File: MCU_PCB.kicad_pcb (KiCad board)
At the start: 2 copper layers, 70 x 70 mm, 51 parts, among them J1 BackBone, J2 D1, J3 D2, J4 Micro_SD_Card, J5 CAM_0, J6 CAM_1, J7 47080-4005, U1 STM32G071GBU, U2 MCP795W22-I/ST, U3 74HCT4051BQ-Q100,1, U4 74HCT4051BQ-Q100,1, U5 ADT7310, U6 LIS2MDLTR, U7 LSM6DSRX, Y1 TG-3541CE

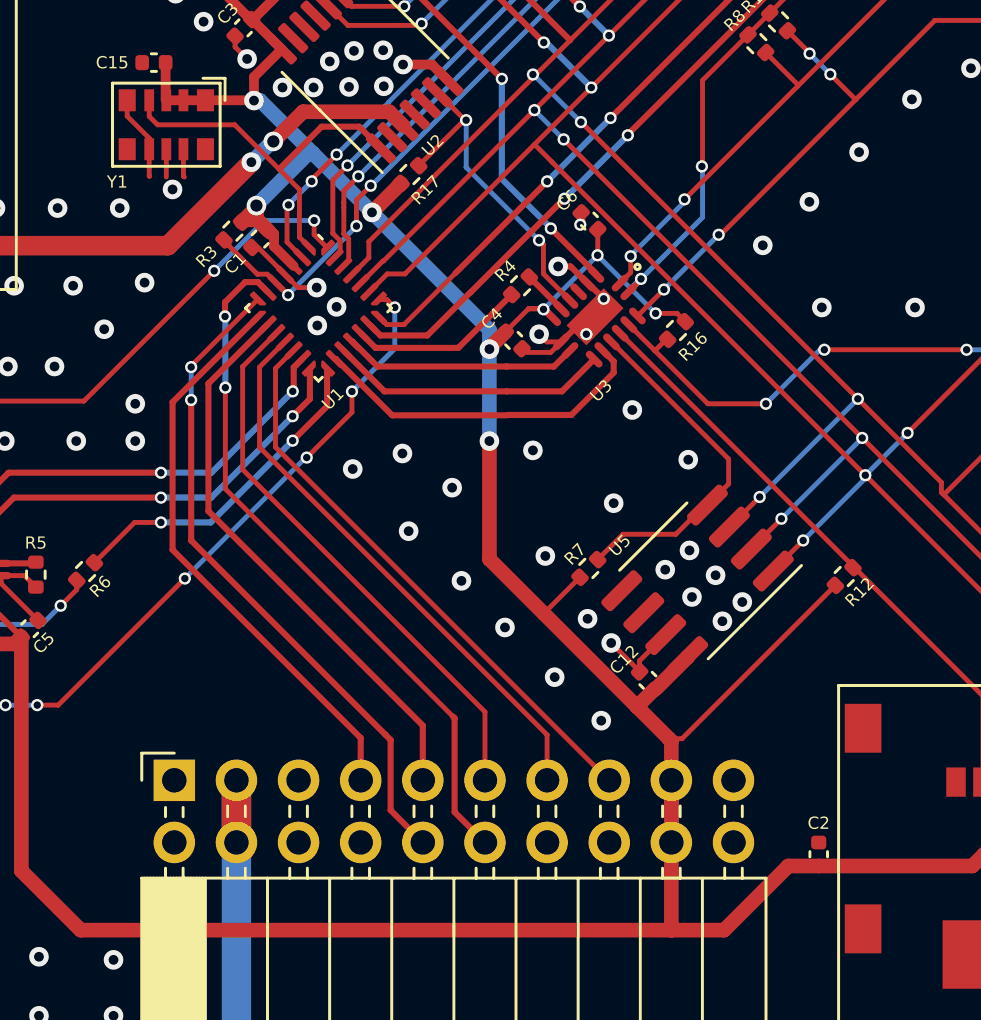
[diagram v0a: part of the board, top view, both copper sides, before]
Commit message: Changed DE-MUX and logic behind it.
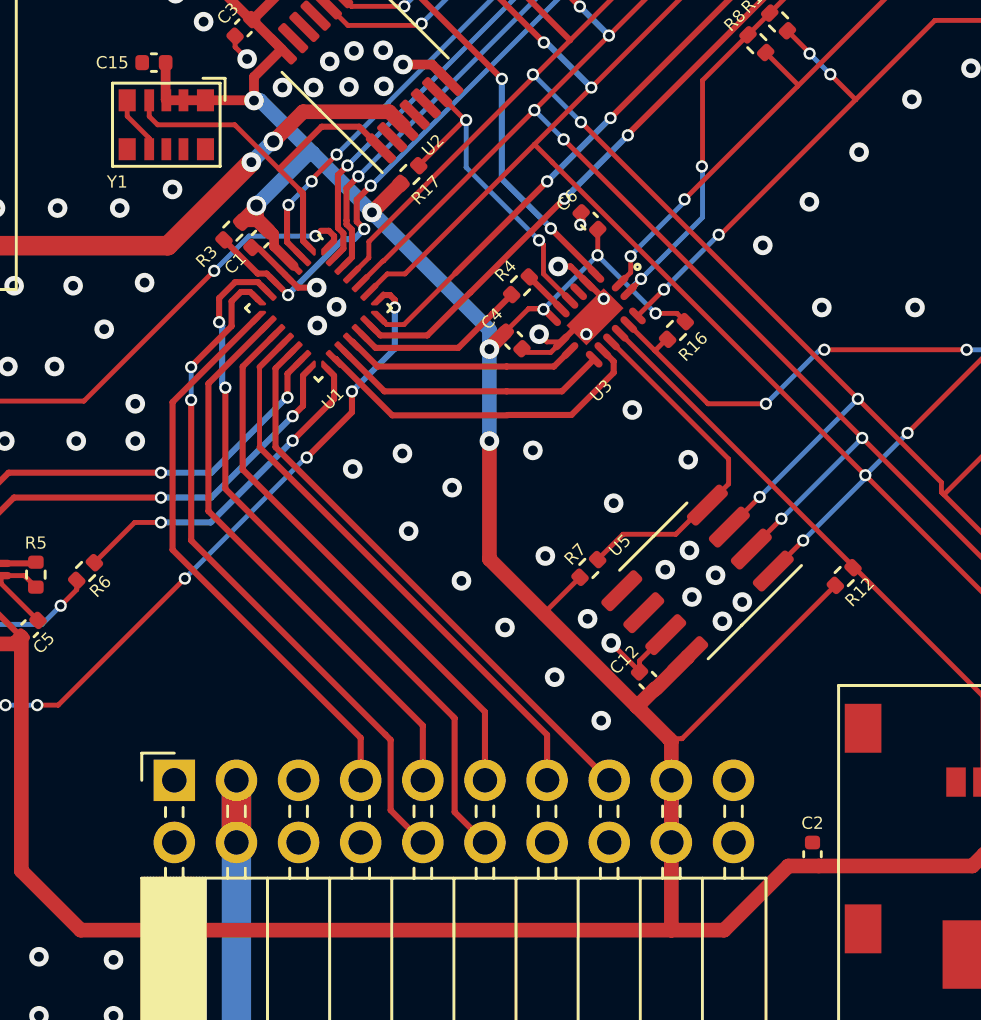
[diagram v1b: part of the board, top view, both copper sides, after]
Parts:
- moved C2 0.25 mm to (142.2, 123.7)
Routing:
- net GND: track 50.3 -> 46.9 mm
- net /IO/COM_RX: track 27.5 -> 28.4 mm
- net /IO/~{RST}: track 36.8 -> 37.5 mm

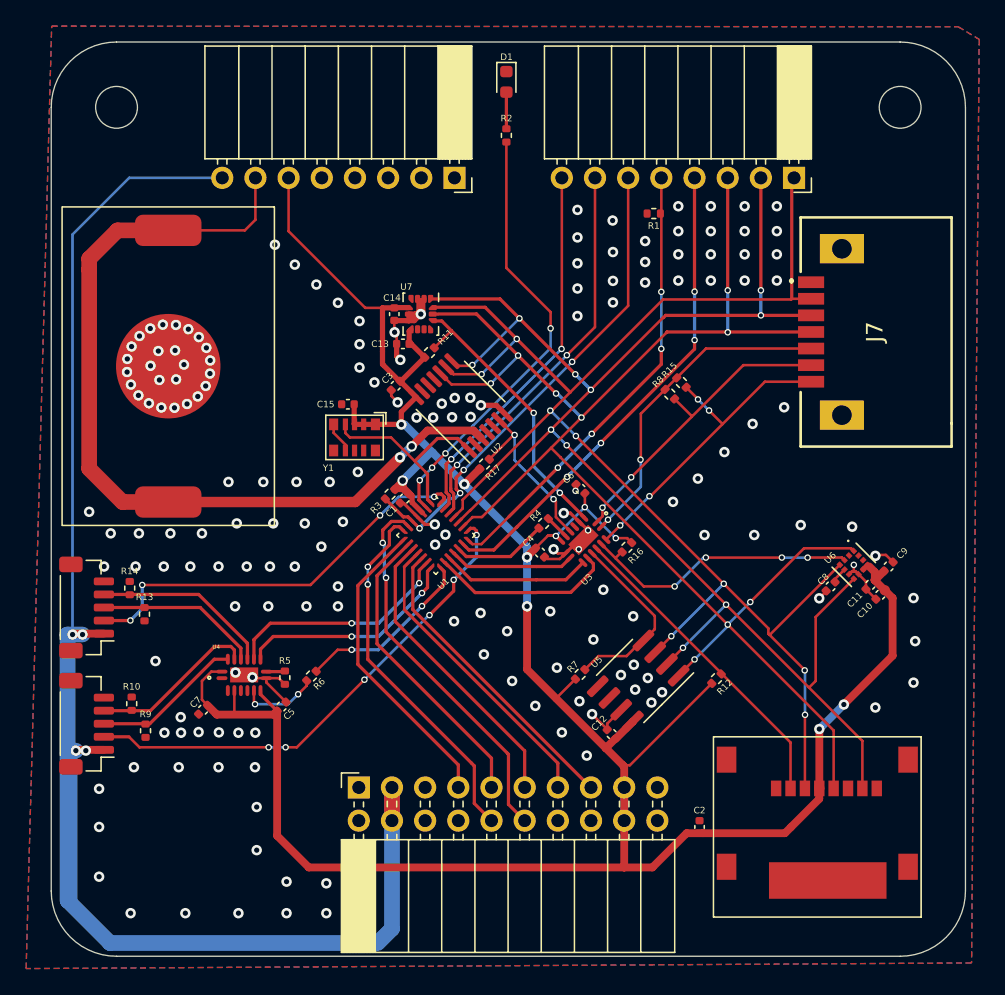
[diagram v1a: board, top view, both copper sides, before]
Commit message: 0.3v KiCad
Needs improvements:
-Visual
-Better grounding
-Component placement
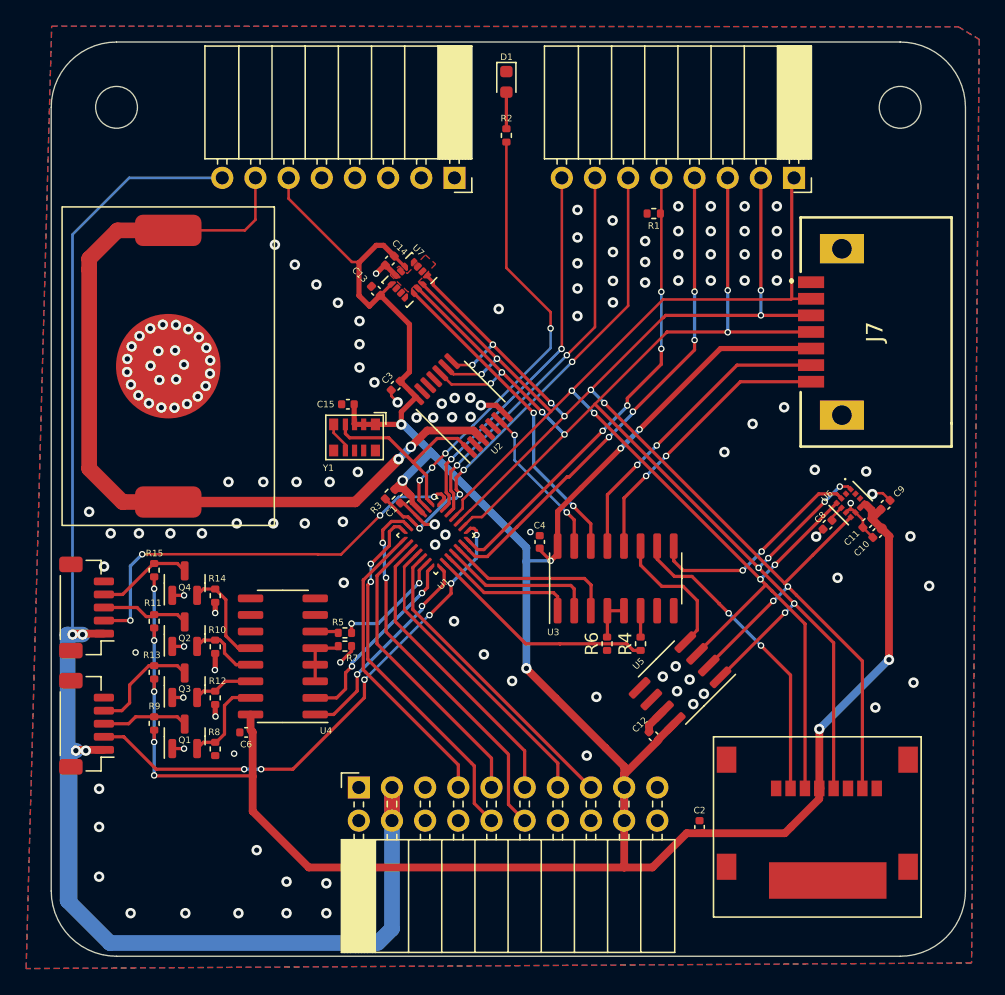
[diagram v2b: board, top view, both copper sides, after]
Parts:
- removed C5, C7: 100nF, Capacitor_SMD:C_0402_1005Metric
- removed R16, R17: 12k, Resistor_SMD:R_0402_1005Metric
- added Q1: RK7002T116, Package_TO_SOT_SMD:SOT-23, F.Cu at (102.8, 116.8)
- added Q2: RK7002T116, Package_TO_SOT_SMD:SOT-23, F.Cu at (102.8, 108.9)
- added Q3: RK7002T116, Package_TO_SOT_SMD:SOT-23, F.Cu at (102.8, 112.8)
- added Q4: RK7002T116, Package_TO_SOT_SMD:SOT-23, F.Cu at (102.8, 105.0)
- U3, U4: value 74HCT4051BQ-Q100,1 -> MC74AC138DR2G; footprint footprints:QFN50P250X350X100-17N -> Package_SO:SOIC-16_3.9x9.9mm_P1.27mm
- moved R8 44.2 mm to (105.2, 117.7), turned to 90 degrees
- moved R15 42.9 mm to (100.5, 104.0), turned to 90 degrees
- moved R12 38.4 mm to (105.2, 113.8), turned to 90 degrees
- moved C6 31.7 mm to (107.5, 116.5), turned to 0 degrees
- moved R11 29.5 mm to (100.5, 108.0), turned to 90 degrees
- moved R6 22.8 mm to (135.2, 109.7), turned to 90 degrees
- moved R7 18.1 mm to (115.1, 109.9), turned to 180 degrees
- moved R4 11.8 mm to (137.7, 109.7), turned to 90 degrees
- moved R10 7.74 mm to (105.2, 109.9), turned to 90 degrees
- moved R14 6.57 mm to (105.2, 106.0), turned to 90 degrees
- moved R5 5.74 mm to (115.1, 108.8), turned to 180 degrees
- moved C10 4.73 mm to (155.8, 101.2)
- moved C11 4.73 mm to (155.1, 100.4)
- moved U6 4.73 mm to (153.8, 98.9)
- moved C8 4.73 mm to (152.0, 100.6)
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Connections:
- C6 pad 1: +3V3 -> GND
- C6 pad 2: GND -> +3V3
- J5 pad 3: /MUX/CAM_ON_0 -> /CAM_SENS/ON/OFF_0
- J5 pad 4: /MUX/CAM_REC_0 -> /CAM_SENS/REC_0
- J6 pad 3: /MUX/CAM_ON_1 -> /CAM_SENS/ON/OFF_1
- J6 pad 4: /MUX/CAM_REC_1 -> /CAM_SENS/REC_1
- J7 pad 6: /MUX/~{BME680_SS} -> /CAM_SENS/~{BME680_SS}
- J7 pad 7: /MUX/~{TEMP_OUT_SS} -> /CAM_SENS/~{TEMP_OUT_SS}
- R10 pad 2: /MUX/CAM_REC_0 -> /MUX/CAM_ON_1_0
- R11 pad 1: /MUX/~{IMU_SS} -> +3V3
- R11 pad 2: +3V3 -> /CAM_SENS/ON/OFF_1
- R12 pad 1: /MUX/~{SD_CARD_SS} -> GND
- R12 pad 2: +3V3 -> /MUX/CAM_REC_0_0
- R13 pad 1: GND -> +3V3
- R13 pad 2: /MUX/CAM_ON_1 -> /CAM_SENS/REC_0
- R14 pad 2: /MUX/CAM_REC_1 -> /MUX/CAM_REC_1_0
- R15 pad 1: /MUX/~{TEMP_OUT_SS} -> +3V3
- R15 pad 2: +3V3 -> /CAM_SENS/REC_1
- R5 pad 1: GND -> /MCU/MUX_EN_1
- R6 pad 1: /MCU/MUX_EN_1 -> GND
- R7 pad 1: /MUX/~{TEMP_IN_SS} -> GND
- R7 pad 2: +3V3 -> Net-(R7-Pad2)
- R8 pad 1: /MUX/~{BME680_SS} -> GND
- R8 pad 2: +3V3 -> /MUX/CAM_ON_0_0
- R9 pad 1: GND -> +3V3
- R9 pad 2: /MUX/CAM_ON_0 -> /CAM_SENS/ON/OFF_0
- U1 pad 13: /MCU/S0_CAM -> /MCU/MUX_EN_1
- U1 pad 15: /MCU/MUX_EN_1 -> /MCU/S0_CAM
- U1 pad 16: /MCU/S0_SENS -> /MCU/MUX_EN_0
- U1 pad 17: /MCU/S1_SENS -> /MCU/S0_SENS
- U1 pad 18: /MCU/S2_SENS -> /MCU/S1_SENS
- U1 pad 19: /MCU/MUX_EN_0 -> /MCU/S2_SENS
- U3 pad 1: /MUX/~{BME680_SS} -> /MCU/S0_SENS
- U3 pad 10: /MCU/S1_SENS -> /MUX/~{SD_CARD_SS}
- U3 pad 11: /MCU/S0_SENS -> /MUX/~{TEMP_IN_SS}
- U3 pad 12: /MUX/~{TEMP_IN_SS} -> /CAM_SENS/~{TEMP_OUT_SS}
- U3 pad 13: /MUX/~{SD_CARD_SS} -> /CAM_SENS/~{BME680_SS}
- U3 pad 14: /MUX/~{MAG_SS} -> /MUX/~{IMU_SS}
- U3 pad 15: /MUX/~{TEMP_OUT_SS} -> /MUX/~{RTC_OUT}
- U3 pad 2: /MUX/~{IMU_SS} -> /MCU/S1_SENS
- U3 pad 3: GND -> /MCU/S2_SENS
- U3 pad 4: unconnected-(U3-Pad4) -> Net-(R6-Pad2)
- U3 pad 5: /MUX/~{RTC_OUT} -> Net-(R6-Pad2)
- U3 pad 7: +3V3 -> unconnected-(U3-Pad7)
- U3 pad 9: /MCU/S2_SENS -> /MUX/~{MAG_SS}
- U4 pad 1: unconnected-(U4-Pad1) -> /MCU/S0_CAM
- U4 pad 10: /MCU/S1_CAM -> unconnected-(U4-Pad10)
- U4 pad 11: /MCU/S0_CAM -> unconnected-(U4-Pad11)
- U4 pad 12: /MUX/CAM_REC_1 -> /MUX/CAM_REC_1_0
- U4 pad 13: /MUX/CAM_ON_1 -> /MUX/CAM_ON_1_0
- U4 pad 14: /MUX/CAM_REC_0 -> /MUX/CAM_REC_0_0
- U4 pad 15: /MUX/CAM_ON_0 -> /MUX/CAM_ON_0_0
- U4 pad 2: unconnected-(U4-Pad2) -> /MCU/S1_CAM
- U4 pad 3: +3V3 -> Net-(R7-Pad2)
- U4 pad 4: unconnected-(U4-Pad4) -> Net-(R7-Pad2)
- U4 pad 5: unconnected-(U4-Pad5) -> Net-(R7-Pad2)
- U4 pad 6: Net-(R6-Pad2) -> Net-(R5-Pad2)
- U4 pad 7: +3V3 -> unconnected-(U4-Pad7)
- U4 pad 9: Net-(R5-Pad2) -> unconnected-(U4-Pad9)
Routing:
- net /MUX/~{TEMP_OUT_SS}: track 24.7 -> 0.00 mm, vias 4 -> 0
- net /MUX/~{BME680_SS}: track 23.7 -> 0.00 mm, vias 2 -> 0
- net /CAM_SENS/~{BME680_SS}: track 0.00 -> 23.6 mm, vias 0 -> 2
- net /CAM_SENS/~{TEMP_OUT_SS}: track 0.00 -> 21.7 mm, vias 0 -> 2
- net GND: track 46.9 -> 27.7 mm, vias 173 -> 138
- net +3V3: track 290.7 -> 272.6 mm, vias 12 -> 13
- net /MUX/CAM_REC_1: track 13.8 -> 0.00 mm
- net /MUX/CAM_REC_0: track 12.8 -> 0.00 mm
- net /MUX/CAM_ON_1: track 12.6 -> 0.00 mm
- net /MUX/CAM_ON_0: track 11.5 -> 0.00 mm
- net /MCU/MUX_EN_0: track 7.33 -> 17.8 mm
- net /CAM_SENS/REC_0: track 0.00 -> 8.65 mm
- net /MUX/CAM_REC_1_0: track 0.00 -> 7.79 mm
- net /CAM_SENS/REC_1: track 0.00 -> 7.40 mm
- net /MUX/CAM_ON_0_0: track 0.00 -> 7.00 mm
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
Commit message: 0.3V KiCad Final version
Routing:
- net +3V3: track 272.6 -> 270.4 mm, vias 13 -> 11
- net GND: track 27.7 -> 26.1 mm, vias 138 -> 216
- net /IO/COM_RX: track 28.4 -> 27.3 mm

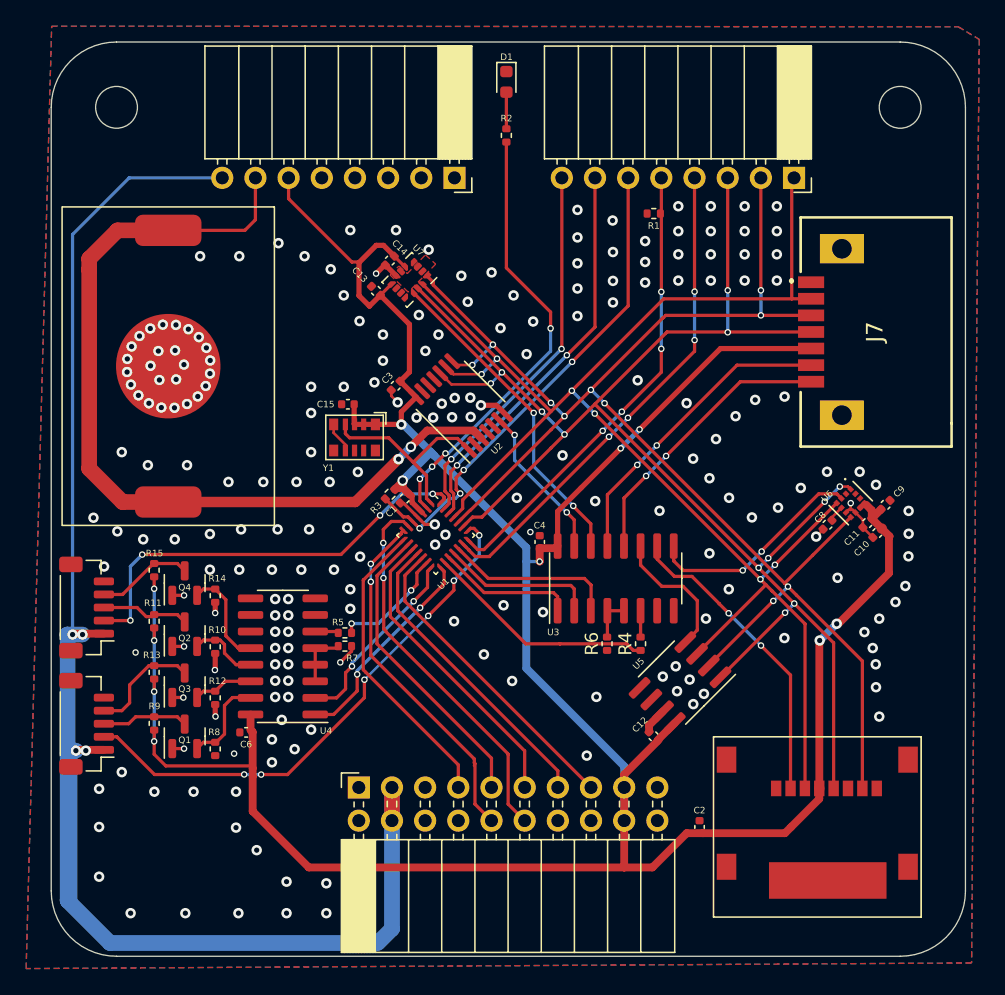
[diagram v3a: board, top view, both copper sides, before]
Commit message: V1
- Corrected SD-cards footprint and schematical represantation;
- Corrected RTC shematics:
	- changed oscilators power supply from internal 3v3 to Vbat so RTC works when PCB is disconnected from external power supply [PWR PCB];
	- 32 kHz to microcontroller now comes from RTC module;
	- added 100 nF decoupling capacitor to Vbat RTC pin.
- Corrected couple connections and component placement on PCB
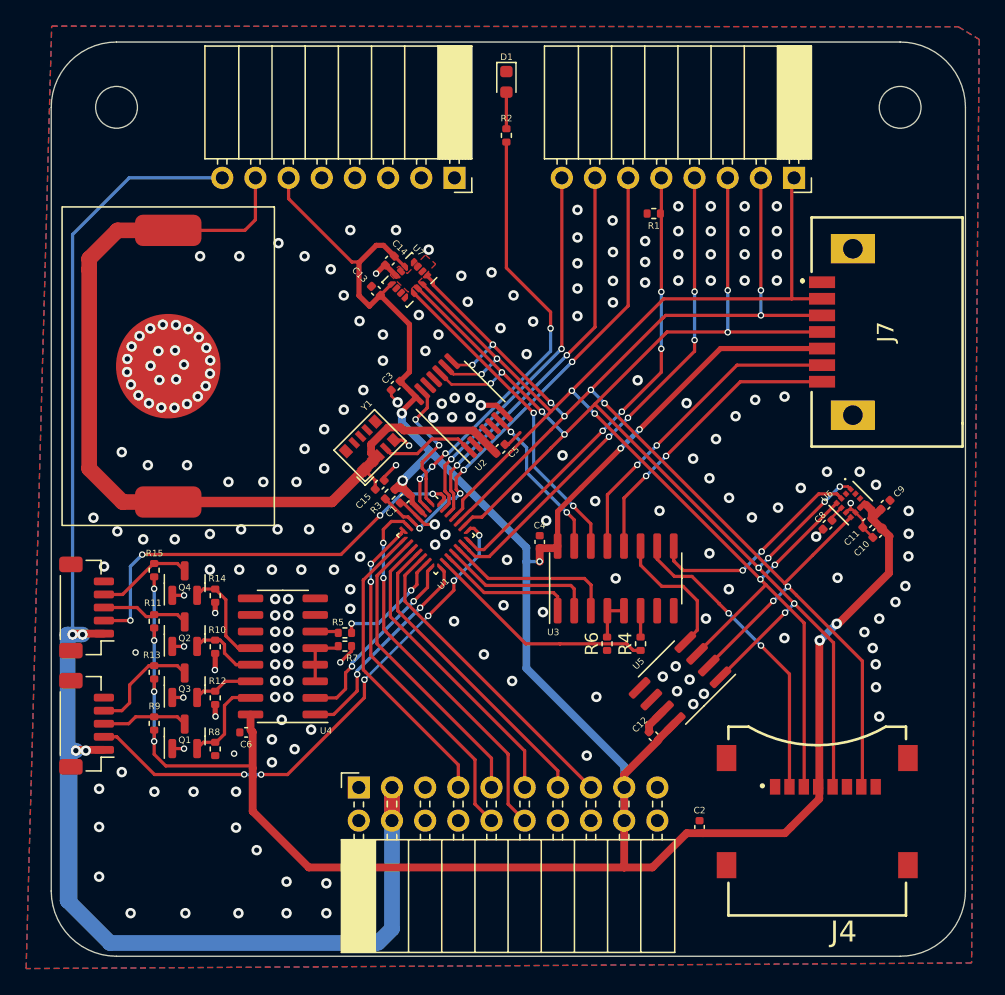
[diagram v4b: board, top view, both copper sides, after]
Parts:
- added C5: 100nF, Capacitor_SMD:C_0402_1005Metric, F.Cu at (127.0, 94.8)
- J4: value Micro_SD_Card -> MEM2067-02-180-00-A_REVB; footprint footprints:Micro_SD -> footprints:GCT_MEM2067-02-180-00-A_REVB
- moved C15 6.63 mm to (117.8, 97.5), turned to 45 degrees
- moved J4 2.64 mm to (151.2, 123.2)
- moved Y1 1.33 mm to (117.0, 94.5), turned to 45 degrees
- moved J7 0.84 mm to (156.5, 85.8)
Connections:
- C15 pad 1: +3V3 -> +BATT
- J5 pad MP: unconnected-(J5-PadMP) -> GND
- J6 pad MP: unconnected-(J6-PadMP) -> GND
- U2 pad 1: /MCU/OSC32_IN -> /RTC/CLK32
- U2 pad 13: unconnected-(U2-Pad13) -> /MCU/OSC32_IN
- Y1 pad 1: +3V3 -> +BATT
- Y1 pad 2: +3V3 -> +BATT
- Y1 pad 3: +3V3 -> +BATT
- Y1 pad 4: /MCU/OSC32_IN -> /RTC/CLK32
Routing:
- net /RTC/CLK32: track 0.00 -> 7.37 mm
- net /MCU/OSC32_IN: track 15.9 -> 10.7 mm, vias 0 -> 2
- net +3V3: track 270.4 -> 265.9 mm
- net +BATT: track 75.4 -> 79.5 mm, vias 2 -> 0
- net GND: track 26.1 -> 28.4 mm, vias 216 -> 217
- net /CAM_SENS/~{TEMP_OUT_SS}: track 21.7 -> 22.5 mm
- net /CAM_SENS/~{BME680_SS}: track 23.6 -> 24.5 mm
- net /CAM_SENS/MISO: track 117.9 -> 118.8 mm
- net /CAM_SENS/CLK: track 120.7 -> 121.5 mm
- net /CAM_SENS/MOSI: track 116.3 -> 116.9 mm
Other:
- board text added: "MADE BY BASEMENT PROJECT WASSUP MCU BOARD V1"
